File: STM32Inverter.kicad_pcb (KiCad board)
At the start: 2 copper layers, 112 parts, among them J1 INTERFACE, J2 RESOLVER, J4 Power, J5 UART, J7 CURRENT SENSE, J8 DRIVER BOARD, Q1 BCX54, Q2 BCX55, Q5 BCX54, Q6 BCX55, U1 STM32F303VCTx, U2 LM358, U3 AD2S1205, U4 74HCT00, U5 74HCT04, U6 74HCT08, U7 MCP2551-I-SN, U8 74HCT08, U9 74HCT08, Y2 CSTNE8M00GH5C000R0, Y3 CSTNE8M00GH5C000R0

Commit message: Schematic cleanup. Pinout changed
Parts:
- removed REF** (x4): MountingHole_4.3mm_M4, MountingHole:MountingHole_4.3mm_M4
- added C17: 100n, Capacitor_SMD:C_0603_1608Metric_Pad1.08x0.95mm_HandSolder, F.Cu at (181.0, 59.0)
- added C29: 100n, Capacitor_SMD:C_0603_1608Metric_Pad1.08x0.95mm_HandSolder, F.Cu at (181.0, 61.5)
- added C30: 100n, Capacitor_SMD:C_0603_1608Metric_Pad1.08x0.95mm_HandSolder, F.Cu at (109.0, 34.0)
- added D4: 1N4007, Diode_SMD:D_SMA_Handsoldering, F.Cu at (208.9, 86.6)
- added D9: PESD3V3L5UY, Package_TO_SOT_SMD:SOT-363_SC-70-6, F.Cu at (207.2, 43.9)
- added F4: 350mA, Fuse:Fuse_0805_2012Metric, F.Cu at (211.9, 42.6)
- added F5: 2A, Fuse:Fuse_0805_2012Metric, F.Cu at (211.9, 45.5)
- added H1: MountingHole_Pad, MountingHole:MountingHole_4.3mm_M4_ISO7380_Pad, F.Cu at (32.0, 42.0)
- added H2: MountingHole_Pad, MountingHole:MountingHole_4.3mm_M4_ISO7380_Pad, F.Cu at (107.0, 49.0)
- added H3: MountingHole_Pad, MountingHole:MountingHole_4.3mm_M4_ISO7380_Pad, F.Cu at (17.0, 107.0)
- added H4: MountingHole_Pad, MountingHole:MountingHole_4.3mm_M4_ISO7380_Pad, F.Cu at (107.0, 107.0)
- added J3: MAIN POWER, Connector_JST:JST_XH_B2B-XH-AM_1x02_P2.50mm_Vertical, F.Cu at (195.3, 86.2)
- added J9: INTERFACE, Connector_IDC:IDC-Header_2x10_P2.54mm_Vertical, F.Cu at (83.0, 18.8)
- added R29: 2.7k, Resistor_SMD:R_0603_1608Metric, F.Cu at (184.8, 71.6)
- added R30: 4.7k, Resistor_SMD:R_0603_1608Metric, F.Cu at (184.8, 74.1)
- added R33: 10k, Resistor_SMD:R_0603_1608Metric_Pad0.98x0.95mm_HandSolder, F.Cu at (185.3, 61.5)
- added R37: 10k, Resistor_SMD:R_0603_1608Metric_Pad0.98x0.95mm_HandSolder, F.Cu at (185.3, 64.0)
- added R38: 10k, Resistor_SMD:R_0603_1608Metric_Pad0.98x0.95mm_HandSolder, F.Cu at (185.3, 66.5)
- added R39: 10k, Resistor_SMD:R_0603_1608Metric_Pad0.98x0.95mm_HandSolder, F.Cu at (189.7, 49.0)
- added R40: 10k, Resistor_SMD:R_0603_1608Metric_Pad0.98x0.95mm_HandSolder, F.Cu at (189.7, 51.5)
- added R41: 2.2k, Resistor_SMD:R_0603_1608Metric_Pad0.98x0.95mm_HandSolder, F.Cu at (189.7, 54.0)
- added R42: 10k, Resistor_SMD:R_0603_1608Metric_Pad0.98x0.95mm_HandSolder, F.Cu at (189.7, 56.5)
- added R43: 2.2k, Resistor_SMD:R_0603_1608Metric_Pad0.98x0.95mm_HandSolder, F.Cu at (189.7, 59.0)
- added R44: 10k, Resistor_SMD:R_0603_1608Metric_Pad0.98x0.95mm_HandSolder, F.Cu at (111.5, 34.0)
- added R45: 2.2k, Resistor_SMD:R_0603_1608Metric_Pad0.98x0.95mm_HandSolder, F.Cu at (114.0, 34.0)
- added U10: ULN2002, Package_SO:SOP-16_3.9x9.9mm_P1.27mm, F.Cu at (102.9, 27.5)
- J1: value INTERFACE -> STLINK; footprint Connector_IDC:IDC-Header_2x10_P2.54mm_Horizontal -> Connector_PinHeader_2.54mm:PinHeader_1x04_P2.54mm_Vertical
- J2: footprint Connector_IDC:IDC-Header_2x06_P2.54mm_Horizontal -> Connector_IDC:IDC-Header_2x06_P2.54mm_Vertical
- J4: footprint Connector_IDC:IDC-Header_2x03_P2.54mm_Horizontal -> Connector_PinHeader_2.54mm:PinHeader_1x06_P2.54mm_Vertical
- J8: footprint Connector_IDC:IDC-Header_2x10_P2.54mm_Horizontal -> Connector_IDC:IDC-Header_2x10_P2.54mm_Vertical
- R18: value R -> 470
- moved J1 179.3 mm to (202.8, 34.6), turned to 0 degrees
- moved U3 109.3 mm to (76.3, 89.0)
- moved C11 81.3 mm to (229.1, 48.3)
- moved C13 81.3 mm to (221.5, 30.5)
- moved C15 81.3 mm to (221.5, 33.0)
- moved C18 81.3 mm to (229.1, 51.3)
- moved C19 81.3 mm to (229.1, 54.3)
- moved C20 81.3 mm to (243.8, 47.6)
- moved D2 81.3 mm to (221.5, 51.2)
- moved D3 81.3 mm to (221.5, 54.2)
- moved D8 81.3 mm to (221.5, 57.1)
- moved JP1 81.3 mm to (249.2, 53.2)
- moved JP2 81.3 mm to (249.2, 56.1)
- moved Q1 81.3 mm to (235.8, 32.2)
- moved Q2 81.3 mm to (235.8, 38.3)
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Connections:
- C21 pad 1: +12V -> +15V
- F3 pad 2: Net-(J1-Pin_12) -> Net-(J9-Pin_16)
- J1 pad 1: +12_EXT -> +3V3
- J1 pad 2: /CAN_H -> unconnected-(J1-Pin_2-Pad2)
- J1 pad 3: +12_EXT -> unconnected-(J1-Pin_3-Pad3)
- J1 pad 4: /CAN_L -> GND
- J4 pad 6: +12V -> Net-(J4-Pin_6)
- U1 pad 72: unconnected-(U1-PA13-Pad72) -> /SWDIO
- U1 pad 76: unconnected-(U1-PA14-Pad76) -> /SWCLK

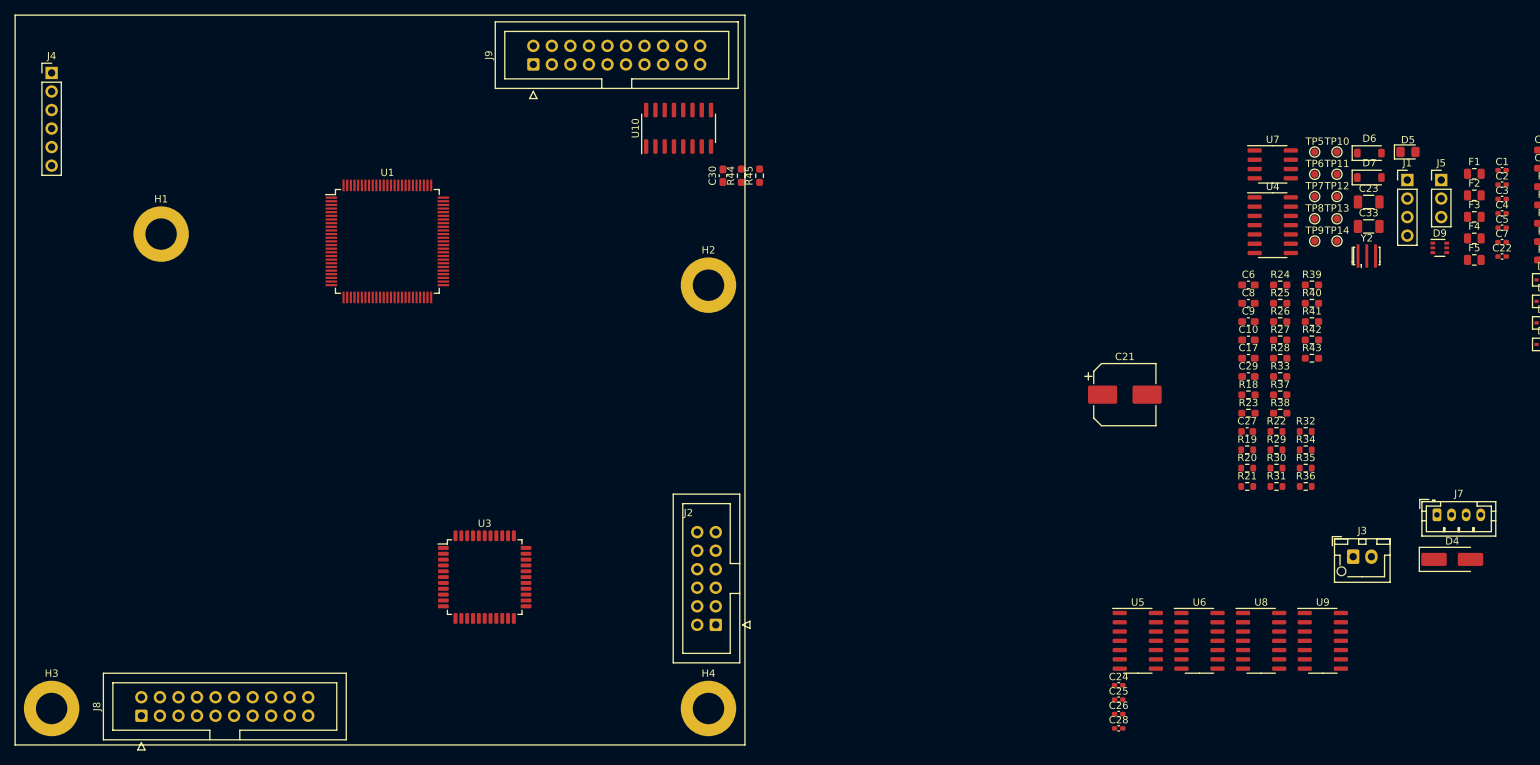
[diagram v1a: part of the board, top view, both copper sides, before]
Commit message: Added libraries, NTC
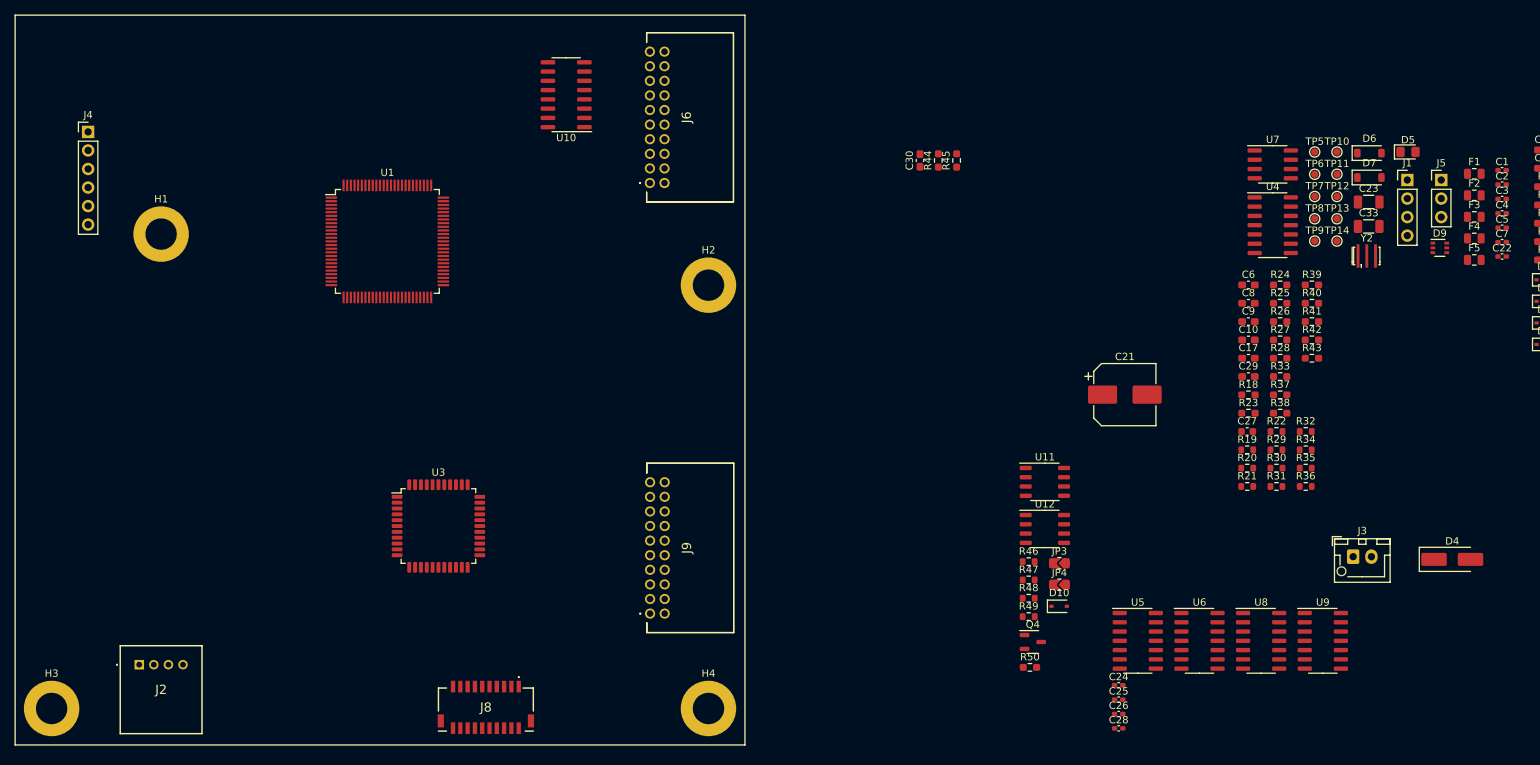
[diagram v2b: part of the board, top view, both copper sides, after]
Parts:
- removed J7: CURRENT SENSE, Connector_JST:JST_PH_B4B-PH-K_1x04_P2.00mm_Vertical
- added D10: 1N4148, Diode_SMD:D_SOD-323, F.Cu at (155.1, 93.0)
- added J6: INTERFACE, DF51-20:DF51K20DP2DS805, F.Cu at (99.0, 35.0)
- added JP3: ~, MEMS_Passive:R_0805_2012Metric_Jumper, F.Cu at (155.1, 87.1)
- added JP4: ~, MEMS_Passive:R_0805_2012Metric_Jumper, F.Cu at (155.1, 90.0)
- added Q4: ST3422A, Package_TO_SOT_SMD:SOT-23-3, F.Cu at (151.4, 97.9)
- added R46: ~, Resistor_SMD:R_0603_1608Metric, F.Cu at (150.9, 86.9)
- added R47: ~, Resistor_SMD:R_0603_1608Metric, F.Cu at (150.9, 89.4)
- added R48: ~, Resistor_SMD:R_0603_1608Metric, F.Cu at (150.9, 91.9)
- added R49: ~, Resistor_SMD:R_0603_1608Metric, F.Cu at (150.9, 94.4)
- added R50: 10k, Resistor_SMD:R_0603_1608Metric_Pad0.98x0.95mm_HandSolder, F.Cu at (151.0, 101.4)
- added U11: LM393, Package_SO:SOP-8_3.9x4.9mm_P1.27mm, F.Cu at (153.1, 76.0)
- added U12: LM393, Package_SO:SOP-8_3.9x4.9mm_P1.27mm, F.Cu at (153.1, 82.4)
- H1: value MountingHole_Pad -> M4
- J2: value RESOLVER -> CURRENT SENSE; footprint Connector_IDC:IDC-Header_2x06_P2.54mm_Vertical -> DF51-4:DF51K4P2DS805
- J8: value DRIVER BOARD -> 501571-2007; footprint Connector_IDC:IDC-Header_2x10_P2.54mm_Vertical -> picoclasp:5015712007
- J9: value INTERFACE -> RESOLVER; footprint Connector_IDC:IDC-Header_2x10_P2.54mm_Vertical -> DF51-20:DF51K20DP2DS805
- moved J2 79.2 mm to (29.0, 101.0), turned to 0 degrees
- moved J9 76.9 mm to (99.0, 94.0)
- moved J8 47.2 mm to (76.5, 107.0), turned to 0 degrees
- moved R44 27.1 mm to (138.5, 31.9)
- moved R45 27.1 mm to (141.0, 31.9)
- moved C30 27.1 mm to (136.0, 31.9)
- moved U10 16.1 mm to (87.5, 22.9), turned to 180 degrees
- moved J4 9.50 mm to (22.0, 28.0)
- moved U3 9.44 mm to (70.0, 82.0)
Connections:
- F3 pad 2: Net-(J9-Pin_16) -> Net-(F3-Pad2)
- J1 pad 2: unconnected-(J1-Pin_2-Pad2) -> /SWDIO
- J1 pad 3: unconnected-(J1-Pin_3-Pad3) -> /SWCLK
- J2 pad 1: /COS_H -> +5V
- J2 pad 2: GND -> /CURRENT_A_RAW
- J2 pad 3: /COS_L -> GND
- J2 pad 4: /TG1 -> /CURRENT_B_RAW
- J9 pad 1: +12_EXT -> /COS_H
- J9 pad 10: GND -> /TH2
- J9 pad 11: /FAN_OUT_OD -> /~{EXC}
- J9 pad 12: /SWDIO -> GND
- J9 pad 13: /PRECHARGE_OUT_OD -> unconnected-(J9-Pad13)
- J9 pad 14: /SWCLK -> unconnected-(J9-Pad14)
- J9 pad 15: /MAIN_OUT_OD -> unconnected-(J9-Pad15)
- J9 pad 16: Net-(J9-Pin_16) -> unconnected-(J9-Pad16)
- J9 pad 17: /X_OUT_OD -> unconnected-(J9-Pad17)
- J9 pad 18: Net-(J9-Pin_18) -> unconnected-(J9-Pad18)
- J9 pad 19: Net-(J9-Pin_19) -> unconnected-(J9-Pad19)
- J9 pad 2: /CAN_H -> GND
- J9 pad 20: Net-(J9-Pin_20) -> unconnected-(J9-Pad20)
- J9 pad 3: +12_EXT -> /COS_L
- J9 pad 4: /CAN_L -> /TG1
- J9 pad 5: GND -> /SIN_H
- J9 pad 6: Net-(J9-Pin_6) -> /TH1
- J9 pad 7: GND -> /SIN_L
- J9 pad 8: Net-(J9-Pin_8) -> /TG2
- J9 pad 9: /PUMP_OUT_OD -> /EXC
- R25 pad 1: Net-(J7-Pin_4) -> /CURRENT_B_RAW
- R27 pad 1: Net-(J7-Pin_2) -> /CURRENT_A_RAW
- R33 pad 1: Net-(J9-Pin_8) -> Net-(J6-Pad8)
- R38 pad 1: Net-(J9-Pin_6) -> Net-(J6-Pad6)
- R40 pad 1: Net-(J9-Pin_18) -> Net-(J6-Pad18)
- R42 pad 1: Net-(J9-Pin_20) -> Net-(J6-Pad20)
- R44 pad 1: Net-(J9-Pin_19) -> Net-(J6-Pad19)
- U10 pad 11: unconnected-(U10-O6-Pad11) -> Net-(Q4-G)
- U10 pad 13: /MAIN_OUT_OD -> unconnected-(U10-O4-Pad13)
- U10 pad 4: /MAIN_OUT -> unconnected-(U10-I4-Pad4)
- U10 pad 5: /X_OUT_OD -> /X_OUT
- U10 pad 6: unconnected-(U10-I6-Pad6) -> /MAIN_OUT
- U4 pad 2: Net-(U4-Pad2) -> /PWM_DRIVER/DRIVER_OUTPUT_ENABLE
- U4 pad 6: Net-(U4-Pad2) -> /PWM_DRIVER/DRIVER_OUTPUT_ENABLE

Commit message: Final version before layout
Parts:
- removed J3: MAIN POWER, Connector_JST:JST_XH_B2B-XH-AM_1x02_P2.50mm_Vertical
- removed J4: Power, Connector_PinHeader_2.54mm:PinHeader_1x06_P2.54mm_Vertical
- added J7: POWER, DF51-8:DF51K8DP2DS805, F.Cu at (81.3, 53.7)
- added R51: 10k, Resistor_SMD:R_0603_1608Metric_Pad0.98x0.95mm_HandSolder, F.Cu at (84.1, 68.0)
- added TH1: Thermistor_NTC, Resistor_SMD:R_0805_2012Metric_Pad1.20x1.40mm_HandSolder, F.Cu at (79.5, 68.2)
- R50: value 10k -> 2.2k
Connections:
- J8 pad MP1: unconnected-(J8-PadMP1) -> GND
- J8 pad MP2: unconnected-(J8-PadMP2) -> GND
- U10 pad 11: Net-(Q4-G) -> unconnected-(U10-O6-Pad11)
- U10 pad 12: /X_OUT_OD -> Net-(Q4-G)
- U10 pad 13: unconnected-(U10-O4-Pad13) -> /X_OUT_OD
- U10 pad 4: unconnected-(U10-I4-Pad4) -> /X_OUT
- U10 pad 5: /X_OUT -> /MAIN_OUT
- U10 pad 6: /MAIN_OUT -> unconnected-(U10-I6-Pad6)

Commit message: Resolver layout
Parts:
- added C31: 1u, Capacitor_SMD:C_0402_1005Metric_Pad0.74x0.62mm_HandSolder, F.Cu at (58.9, 78.2)
- added D11: BZT52C3V6, Diode_SMD:D_SOD-123, F.Cu at (200.0, 62.4)
- added D12: BZT52C3V6, Diode_SMD:D_SOD-123, F.Cu at (200.0, 65.8)
- added R52: 10k, Resistor_SMD:R_0603_1608Metric_Pad0.98x0.95mm_HandSolder, F.Cu at (205.1, 62.0)
- added R53: 10k, Resistor_SMD:R_0603_1608Metric_Pad0.98x0.95mm_HandSolder, F.Cu at (205.1, 64.5)
- C11, C18, C19: footprint Capacitor_SMD:C_0805_2012Metric_Pad1.18x1.45mm_HandSolder -> Capacitor_SMD:C_0603_1608Metric_Pad1.08x0.95mm_HandSolder
- TP2, TP3: moved to B.Cu
- moved C12 189.8 mm to (66.6, 91.3), turned to -90 degrees
- moved C16 187.9 mm to (64.4, 73.7), turned to 90 degrees
- moved C14 185.0 mm to (67.6, 73.7), turned to 90 degrees
- moved Q6 180.5 mm to (64.0, 106.0), turned to -90 degrees
- moved R15 179.5 mm to (62.9, 100.5), turned to 180 degrees
- moved JP1 174.8 mm to (76.9, 82.5)
- moved Q5 174.1 mm to (73.0, 106.0), turned to -90 degrees
- moved JP2 173.6 mm to (76.9, 76.8)
- moved R9 171.9 mm to (67.5, 104.9), turned to 90 degrees
- moved Q2 170.8 mm to (79.0, 106.0), turned to -90 degrees
- moved R14 170.2 mm to (74.0, 100.5), turned to 180 degrees
- moved C19 167.4 mm to (69.5, 104.9), turned to 90 degrees
- moved Y3 167.4 mm to (71.5, 91.9)
- moved U2 165.6 mm to (82.0, 94.5)
- moved Q1 165.1 mm to (88.0, 106.0), turned to -90 degrees
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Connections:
- J9 pad 4: /TG1 -> GND
- J9 pad 8: /TG2 -> GND
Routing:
- net +15V: track 0.00 -> 74.0 mm
- net /EXC: track 0.00 -> 64.7 mm, vias 0 -> 1
- net /COS_H: track 0.00 -> 57.1 mm, vias 0 -> 2
- net /COS_L: track 0.00 -> 52.4 mm, vias 0 -> 2
- net /SIN_H: track 0.00 -> 45.9 mm, vias 0 -> 2
- net /SIN_L: track 0.00 -> 45.9 mm, vias 0 -> 2
- net Net-(U2B--): track 0.00 -> 42.0 mm, vias 0 -> 1
- net /~{EXC}: track 0.00 -> 41.5 mm, vias 0 -> 2
- net +5V: track 0.00 -> 38.4 mm
- net /AD2S1205/EXC: track 0.00 -> 35.6 mm, vias 0 -> 2
- net Net-(D1-A): track 0.00 -> 27.3 mm, vias 0 -> 2
- net Net-(U2A--): track 0.00 -> 24.7 mm, vias 0 -> 2
- net Net-(D2-K): track 0.00 -> 21.2 mm, vias 0 -> 1
- net GND: track 0.00 -> 20.1 mm, vias 0 -> 1
- net /AD2S1205/~{EXC}: track 0.00 -> 18.8 mm, vias 0 -> 2
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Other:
- copper layers 2 -> 4

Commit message: Key exclusion layout
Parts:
- moved C1 162.8 mm to (53.2, 42.0), turned to 180 degrees
- moved C2 158.2 mm to (59.0, 56.6), turned to -90 degrees
- moved C5 157.9 mm to (58.0, 33.7), turned to 90 degrees
- moved U9 156.4 mm to (35.0, 89.5)
- moved U6 150.3 mm to (24.2, 89.6)
- moved U8 147.8 mm to (36.5, 76.5)
- moved C3 147.0 mm to (70.0, 56.6), turned to -90 degrees
- moved U5 143.2 mm to (24.2, 76.4)
- moved C25 140.8 mm to (24.2, 83.3)
- moved C4 140.2 mm to (75.6, 39.2)
- moved C24 137.5 mm to (29.3, 72.6)
- moved C28 130.8 mm to (35.1, 83.2)
- moved C26 126.1 mm to (42.1, 72.6)
- moved R52 117.1 mm to (89.0, 77.5), turned to -90 degrees
- moved R53 112.8 mm to (93.0, 77.5), turned to -90 degrees
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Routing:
- net /PWM_DRIVER/DRIVER_OUTPUT_ENABLE: track 0.00 -> 33.7 mm, vias 0 -> 6
- net Net-(U5-Pad13): track 0.00 -> 32.5 mm, vias 0 -> 4
- net Net-(U5-Pad5): track 0.00 -> 32.3 mm, vias 0 -> 5
- net Net-(U5-Pad3): track 0.00 -> 32.0 mm, vias 0 -> 4
- net Net-(U5-Pad1): track 0.00 -> 29.8 mm, vias 0 -> 2
- net Net-(U5-Pad9): track 0.00 -> 28.8 mm, vias 0 -> 4
- net Net-(U5-Pad11): track 0.00 -> 26.7 mm, vias 0 -> 4
- net Net-(U5-Pad10): track 0.00 -> 17.2 mm, vias 0 -> 2
- net Net-(U5-Pad12): track 0.00 -> 16.2 mm, vias 0 -> 2
- net Net-(U5-Pad8): track 0.00 -> 14.1 mm, vias 0 -> 2
- net Net-(U5-Pad4): track 0.00 -> 13.2 mm, vias 0 -> 2
- net Net-(U5-Pad2): track 0.00 -> 12.5 mm, vias 0 -> 2
- net Net-(U5-Pad6): track 0.00 -> 12.1 mm, vias 0 -> 2
- net Net-(R20-Pad1): track 0.00 -> 7.66 mm
- net Net-(U4-Pad11): track 0.00 -> 5.48 mm
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
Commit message: Layout mostly done
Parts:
- R31, R32, R34, R35, R36, TP10, TP11, TP12, TP13, TP14, TP5, TP6, TP7, TP8, TP9: moved to B.Cu
- U11, U12: footprint Package_SO:SOP-8_3.9x4.9mm_P1.27mm -> Package_SO:SO-8_3.9x4.9mm_P1.27mm
- moved F4 183.2 mm to (30.0, 21.2), turned to 180 degrees
- moved F2 183.0 mm to (30.0, 16.8), turned to 180 degrees
- moved F1 182.5 mm to (30.0, 19.0), turned to 180 degrees
- moved R28 174.2 mm to (15.2, 96.6), turned to -90 degrees
- moved R27 174.0 mm to (15.2, 93.1), turned to -90 degrees
- moved R26 173.6 mm to (15.2, 88.6), turned to -90 degrees
- moved R25 173.4 mm to (15.2, 85.1), turned to -90 degrees
- moved TP5 167.2 mm to (40.4, 105.2), turned to -90 degrees
- moved TP10 165.0 mm to (42.6, 98.3), turned to -90 degrees
- moved TP6 163.1 mm to (43.5, 105.2), turned to -90 degrees
- moved C7 162.6 mm to (53.2, 49.2), turned to 180 degrees
- moved C22 162.2 mm to (54.3, 61.2)
- moved TP11 161.0 mm to (45.6, 98.3), turned to -90 degrees
- moved TP7 160.2 mm to (43.8, 102.0), turned to -90 degrees
- moved TP12 156.9 mm to (48.7, 98.3), turned to -90 degrees
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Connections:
- J6 pad 1: +12_EXT -> Net-(J6-Pad1)
- J6 pad 11: /FAN_OUT_OD -> /X_OUT_OD
- J6 pad 13: /PRECHARGE_OUT_OD -> GND
- J6 pad 15: /MAIN_OUT_OD -> GND
- J6 pad 17: /X_OUT_OD -> +12_EXT
- J6 pad 19: Net-(J6-Pad19) -> +12_EXT
- J6 pad 3: +12_EXT -> /PUMP_OUT_OD
- J6 pad 5: GND -> /FAN_OUT_OD
- J6 pad 7: GND -> /PRECHARGE_OUT_OD
- J6 pad 9: /PUMP_OUT_OD -> /MAIN_OUT_OD
- R44 pad 1: Net-(J6-Pad19) -> Net-(J6-Pad1)
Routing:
- net +5V: track 43.0 -> 151.0 mm, vias 0 -> 2
- net +12_UNSTABILIZED: track 0.00 -> 98.0 mm
- net /FAULT_DRV: track 0.00 -> 55.6 mm, vias 0 -> 4
- net /CURRENT_A_RAW: track 0.00 -> 44.4 mm, vias 0 -> 4
- net Net-(J6-Pad18): track 0.00 -> 44.1 mm, vias 0 -> 1
- net Net-(J6-Pad20): track 0.00 -> 41.5 mm, vias 0 -> 1
- net /TH1: track 0.00 -> 39.7 mm, vias 0 -> 2
- net Net-(J6-Pad8): track 0.00 -> 38.7 mm
- net /CURRENT_B_RAW: track 0.00 -> 38.4 mm, vias 0 -> 4
- net Net-(J6-Pad6): track 0.00 -> 38.1 mm
- net /NEG_CURRENT_SETPOINT: track 0.00 -> 28.4 mm, vias 0 -> 3
- net /TH2: track 0.00 -> 27.9 mm, vias 0 -> 2
- net Net-(J6-Pad14): track 0.00 -> 26.7 mm
- net /PRECHARGE_OUT_OD: track 0.00 -> 24.6 mm, vias 0 -> 1
- net Net-(F3-Pad2): track 0.00 -> 23.5 mm, vias 0 -> 1
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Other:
- board outline added: 100 x 100 mm

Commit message: Traces almost done
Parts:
- moved R23 54.8 mm to (38.3, 26.0)
- moved R24 54.8 mm to (42.3, 26.0)
- moved R18 45.4 mm to (69.4, 28.5)
- moved D5 45.4 mm to (65.3, 28.5)
- moved J5 40.7 mm to (107.0, 62.5), turned to 180 degrees
- moved JP4 39.1 mm to (78.7, 32.0)
- moved JP3 39.0 mm to (78.7, 29.5)
- moved TH1 28.4 mm to (65.2, 32.8), turned to 180 degrees
- moved R51 28.2 mm to (69.6, 32.8), turned to 180 degrees
- moved J1 18.4 mm to (63.6, 18.0)
- moved D9 17.4 mm to (84.8, 53.2)
- moved R50 15.4 mm to (82.3, 32.0), turned to 0 degrees
- moved TP2 15.1 mm to (79.2, 82.8)
- moved TP8 15.1 mm to (58.5, 108.8)
- moved TP11 12.0 mm to (56.5, 93.2)
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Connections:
- D9 pad 4: /KEY_IN -> /AUX_IN
- D9 pad 6: /AUX_IN -> /KEY_IN
- U1 pad 15: unconnected-(U1-PC0-Pad15) -> /CURRENT_A
- U1 pad 16: unconnected-(U1-PC1-Pad16) -> /2.5V
- U1 pad 17: unconnected-(U1-PC2-Pad17) -> /CURRENT_B
- U1 pad 18: unconnected-(U1-PC3-Pad18) -> /2.5V
- U1 pad 19: unconnected-(U1-PF2-Pad19) -> /T3_DRV
- U1 pad 26: unconnected-(U1-PA3-Pad26) -> /T2_DRV
- U1 pad 27: unconnected-(U1-PF4-Pad27) -> /T1_DRV
- U1 pad 39: unconnected-(U1-PE8-Pad39) -> /TH1
- U1 pad 45: unconnected-(U1-PE14-Pad45) -> /TH2
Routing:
- net +15V: track 74.0 -> 214.7 mm, vias 0 -> 2
- net +5VA: track 0.00 -> 127.5 mm, vias 0 -> 3
- net +3V3: track 19.4 -> 114.1 mm, vias 0 -> 16
- net /CURRENT_A: track 1.67 -> 92.7 mm, vias 0 -> 3
- net /CURRENT_B: track 1.67 -> 82.8 mm, vias 0 -> 3
- net /PWM_CH1N: track 0.00 -> 78.1 mm, vias 0 -> 5
- net /PWM_CH2: track 0.00 -> 71.7 mm, vias 0 -> 4
- net /T3_DRV: track 8.42 -> 79.9 mm, vias 1 -> 3
- net /PWM_CH1: track 0.00 -> 64.5 mm, vias 0 -> 4
- net /T1_DRV: track 8.17 -> 72.6 mm, vias 1 -> 3
- net /T2_DRV: track 3.67 -> 65.8 mm, vias 1 -> 3
- net /PWM_CH2N: track 0.00 -> 54.6 mm, vias 0 -> 3
- net /CS_RES: track 0.00 -> 52.9 mm, vias 0 -> 5
- net /TH2: track 27.9 -> 77.4 mm, vias 2 -> 5
- net /V_LOW: track 0.00 -> 49.0 mm, vias 0 -> 4
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- added copper zone on In2.Cu, net +3V3
- added copper zone on In2.Cu, net +5V
- added copper zone on F.Cu, net GND
- added copper zone on In1.Cu, net GND
